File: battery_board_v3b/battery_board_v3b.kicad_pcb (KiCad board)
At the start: 4 copper layers, 88 x 94.5 mm, 205 parts, among them IC2 PCT2075DP,118, IC3 RP2040_QFN56, IC4 LT3652IMSE#PBF, J1 Bypass, J10 Jetson, J11 BM04B-SRSS-TB(LF)(SN), J12 FC_FACE, J14 Solar, J15 FC, J16 I2C Multiplexer Breakout, J17 ISS Foot, J18 Screw_Terminal_01x02, J19 BM04B-SRSS-TB(LF)(SN), J20 CAN1, J21 BM04B-SRSS-TB(LF)(SN), J22 CAN2, J23 Conn_ARM_JTAG_SWD_10, J24 USB_B_Micro, J25 Life Makes Lemonade, J26 BM04B-SRSS-TB(LF)(SN), J27 I2C0 Breakout, J3 Heater, J4 CHARGE, J5 Foot0, J6 Foot1, J7 Foot2, J8 Foot3, J9 RBF, K1 APAN3105, Q1 IRF7458, Q10 IRLML2803, Q11 NDS8434, Q2 IRF7458, Q3 MBT2222ADW1T1, Q4 MMBT2222AT, Q5 MBT2222ADW1T1, Q6 IRLML2803, Q7 IRLML2803, Q8 NDS8434, Q9 NDS8434, SW1 KMR2, SW2 KMR2, U1 R5460N208AA, U10 TLVH431 DBZ SOT-23, U11 MCP25625-E/ML, U12 INA219AxD, U13 MAX706RESA, U14 INA219AxD, U2 1049, U3 TPS54226PWPRPWP14_2P31X2P46-L, U4 1049, U5 TPS54226PWPRPWP14_2P31X2P46-L, U6 TPS7A4501DCQT, U7 ADS1015IDGS, U8 W25Q128JV, U9 AD8495, Y1 Crystal_GND24, Y2 Crystal_GND24

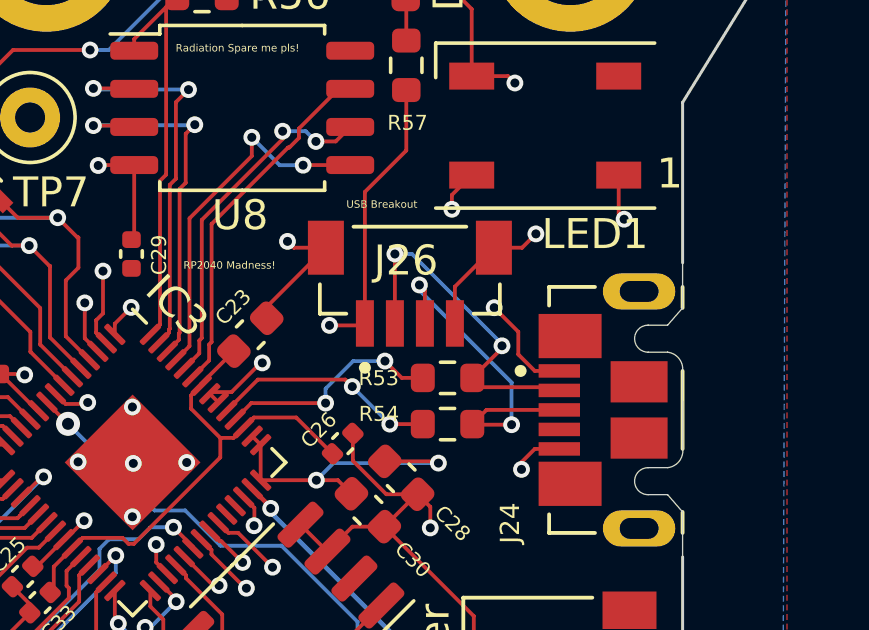
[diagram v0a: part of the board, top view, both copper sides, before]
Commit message: Updated USB passthrough routing
Changed pass through to go through the JST conenctor
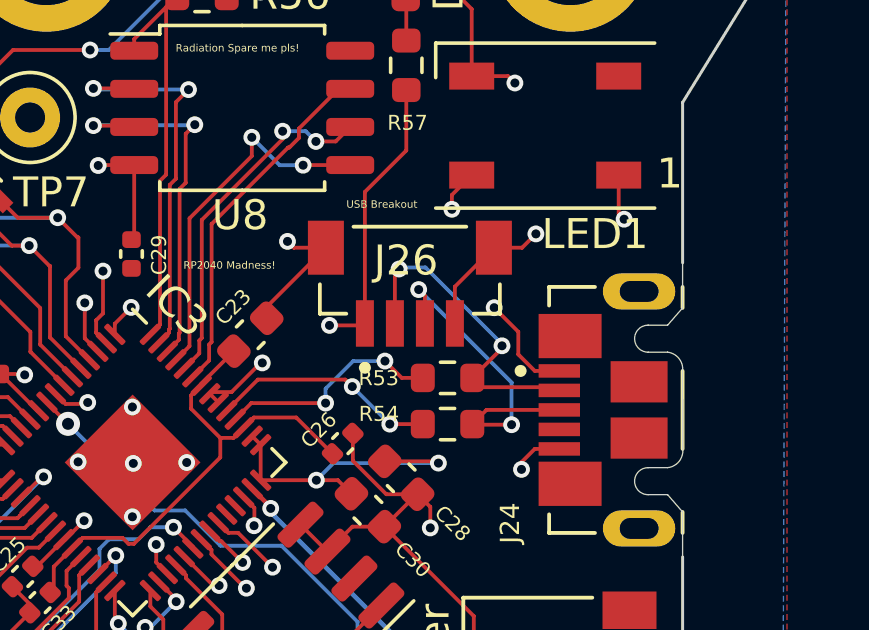
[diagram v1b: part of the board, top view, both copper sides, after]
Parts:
- J12: value FC_FACE -> Z+_Cap_Connector
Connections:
- J12 pad 6: USB_D+ -> D-
- J12 pad 7: USB_D- -> D+
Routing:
- net D+: track 11.7 -> 95.5 mm, vias 2 -> 4
- net D-: track 11.7 -> 93.9 mm, vias 2 -> 4
- net USB_D+: track 87.3 -> 7.58 mm, vias 4 -> 2
- net USB_D-: track 87.0 -> 7.57 mm, vias 4 -> 2

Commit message: As Ordered June 12, 2024
V3b finished. Recent additions:
- Direct Change Port on the 12-Pin Picolock
- Aligned charge circuit with FlatSat Dev design
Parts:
- removed J4: CHARGE, Battery Board:MOLEX_504050-0291
- added D11: DFLS130L-7, Diode_SMD:D_PowerDI-123, F.Cu at (165.8, 115.5)
- added D12: DFLS130L-7, Diode_SMD:D_PowerDI-123, F.Cu at (165.3, 97.1)
- added R1043: 100K, Resistor_SMD:R_0603_1608Metric, F.Cu at (167.9, 116.5)
- R43: value 200k -> 100k
- R44: value 85k -> 94k
- moved J14 8.45 mm to (191.9, 103.4)
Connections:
- C34 pad 1: Net-(D4-K) -> Net-(D11-K)
- D4 pad 1: Net-(D4-K) -> Net-(D11-K)
- IC4 pad 1: Net-(D4-K) -> Net-(D11-K)
- IC4 pad 3: Net-(D4-K) -> Net-(D11-K)
- J12 pad 4: GND -> Dir_Chrg_In
- R43 pad 1: Net-(D4-K) -> Net-(R1043-Pad2)
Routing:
- net Dir_Chrg_In: track 0.00 -> 125.0 mm, vias 0 -> 3
- net PACK-: track 97.6 -> 55.3 mm, vias 5 -> 3
- net Net-(D11-K): track 0.00 -> 28.2 mm
- net Net-(D4-K): track 22.4 -> 0.00 mm
- net VBATT_SENSE: track 42.2 -> 33.2 mm
- net VSOLAR: track 11.8 -> 20.3 mm
- net SDA0: track 162.9 -> 158.4 mm
- net VBatt: track 78.1 -> 80.4 mm
- net SCL0: track 162.3 -> 164.3 mm
- net Net-(R1043-Pad2): track 0.00 -> 1.52 mm
- net GND: track 321.2 -> 319.9 mm, vias 66 -> 65
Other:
- board text added: "WDT Enable"
- board text removed: "Direct Charge Port"
- board text removed: "R45 is WDT Enable"
